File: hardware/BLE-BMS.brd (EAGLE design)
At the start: 61 x 50.8 mm, 88 parts, among them Q1 BSS138, U1 BQ7694040

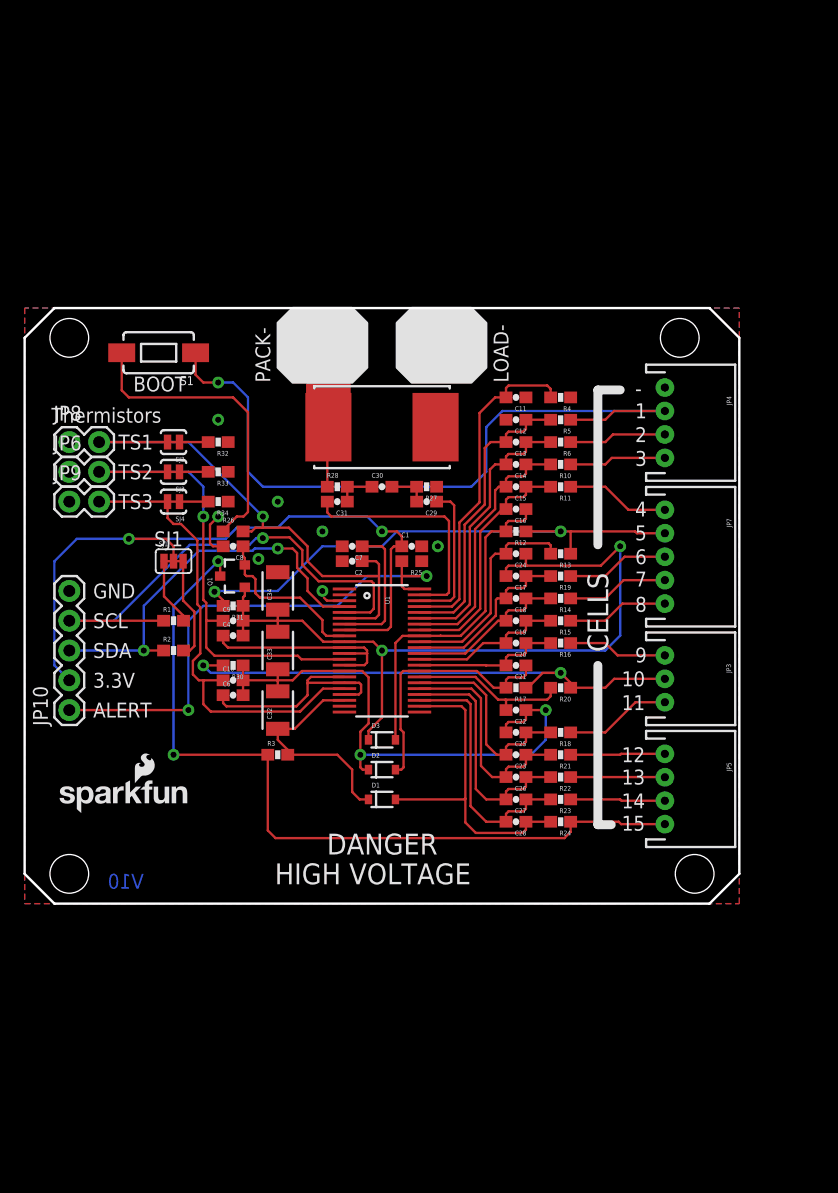
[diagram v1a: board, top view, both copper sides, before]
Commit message: v2 with Charge/Discharge MOSFET control and cell balancing
Many changes. Added large MOSFETs and pack interface circuitry. Added
small MOSFETs for individual cell balancing/charging. Corrected
Thermistor pull down error. All FPs pass 1:1 check.
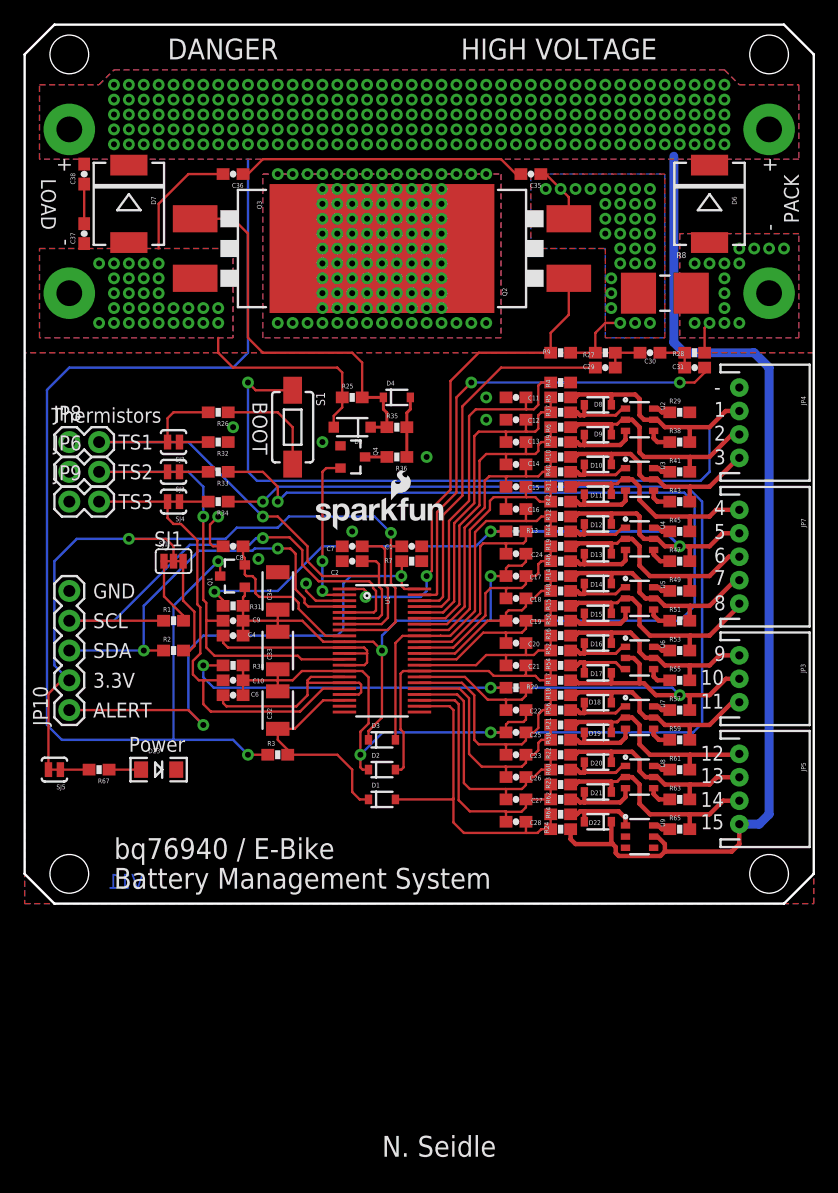
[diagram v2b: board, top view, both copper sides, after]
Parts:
- added C35, C36, C37, C38: 0.1uF, SparkFun-Capacitors:0603-CAP
- added D10, D11, D12, D13, D14, D15, D16, D17, D18, D19, D20, D21, D22, D8, D9: 5.6V, SparkFun-DiscreteSemi:SOD-323
- added D23: RED, SparkFun-LED:LED-1206
- added D4: BAS16, SparkFun-DiscreteSemi:SOD-323
- added D5: MMSZ5246B-7-F, SparkFun-DiscreteSemi:SOD-123
- added D6: SMCJ75AFS, SparkFun-DiscreteSemi:SMC
- added D7: ES3J, SparkFun-DiscreteSemi:SMC
- added Q2, Q3: PSMN7R0-100BS, SparkFun-DiscreteSemi:TO-263/D2PAK
- added Q4: 30V, 2.5A, SparkFun-DiscreteSemi:SOT23-3
- added R35, R7, R9: 1M, SparkFun-Resistors:0603-RES
- added R36, R67: 1K, SparkFun-Resistors:0603-RES
- added R37, R39, R40, R42, R44, R46, R48, R50, R52, R54, R56, R58, R60, R62, R64: 10K, SparkFun-Resistors:0603-RES
- added R38, R41, R43, R45, R47, R49, R51, R53, R55, R57, R59, R61, R63, R65: 100/.25W, SparkFun-Resistors:0603-RES
- added R8: CSR2512C0R001F, bq769x0:2512
- added SJ5: (no value), SparkFun-Passives:PAD-JUMPER-2-NC_BY_TRACE_YES_SILK
- added U2, U3, U4, U5, U6, U7, U8, U9: DMP2240, SparkFun-DiscreteSemi:SOT26
- R25: value 4.7k -> 1M; device SparkFun-Resistors:0603 -> SparkFun-Resistors:0603-RES
- R26: device SparkFun-Resistors:0603 -> SparkFun-Resistors:0603-RES
- R29: value .001 -> 100/.25W; device bq769x0:4527 -> SparkFun-Resistors:0603-RES
- U1: value BQ7694040 -> bq7694002DBT
- moved U$7 59.3 mm to (13.6, 2.08)
- moved C31 32.6 mm to (57.1, 45.7), turned to 0 degrees
- moved R28 32.6 mm to (57.1, 47.0), turned to 180 degrees
- moved LOGO1 32.5 mm to (24.4, 31.8)
- moved C30 25.6 mm to (53.3, 47.0), turned to 180 degrees
- moved R29 25.4 mm to (55.9, 41.9), turned to 0 degrees
- moved STANDOFF4 25.3 mm to (63.5, 72.4)
- moved STANDOFF3 24.2 mm to (3.81, 72.4)
- moved C29 19.1 mm to (49.5, 45.7), turned to 0 degrees
- moved R27 19.1 mm to (49.5, 47.0), turned to 0 degrees
- moved R25 14.9 mm to (27.9, 43.2), turned to 0 degrees
- moved S1 13.1 mm to (22.9, 40.6), turned to 270 degrees
- moved R26 10.2 mm to (16.5, 41.9), turned to 180 degrees
- moved JP3 6.35 mm to (61.0, 19.2)
- moved JP4 6.35 mm to (61.0, 41.0)
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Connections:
- removed net PACK-: R28.1, R29.2
- new net CHG_CTL: D4.C, D5.C, Q3.1, R25.2, R35.1
- new net LOAD-: C36.2, C37.1, D5.A, D7.A, Q3.3, R25.1
- new net LOAD1: Q2.2, Q3.2
- new net LOAD2: C35.1, Q2.3, R27.1, R8.1, R9.1
- new net N$1: D8.A, R37.1, U2.G1
- new net N$12: D10.A, R40.1, U3.G1
- new net N$13: R41.1, U3.D1
- new net N$14: D11.A, R42.1, U3.G2
- new net N$16: R43.1, U3.D2
- new net N$18: D12.A, R44.1, U4.G1
- new net N$19: R45.1, U4.D1
- new net N$2: Q4.3, R36.2
- new net N$20: D13.A, R46.1, U4.G2
- new net N$21: R47.1, U4.D2
- new net N$23: R49.1, U5.D1
- new net N$25: D14.A, R48.1, U5.G1
- new net N$26: R51.1, U5.D2
- new net N$27: D15.A, R50.1, U5.G2
- new net N$37: R53.1, U6.D1
- new net N$38: D16.A, R52.1, U6.G1
- new net N$39: D17.A, R54.1, U6.G2
- new net N$4: R29.1, U2.D1
- new net N$41: R55.1, U6.D2
- new net N$42: D18.A, R56.1, U7.G1
- new net N$43: R57.1, U7.D1
- new net N$44: D19.A, R58.1, U7.G2
- new net N$46: R59.1, U7.D2
- new net N$47: D20.A, R60.1, U8.G1
- new net N$5: D9.A, R39.1, U2.G2
- new net N$50: R61.1, U8.D1
- new net N$51: D21.A, R62.1, U8.G2
- new net N$52: R63.1, U8.D2
- new net N$53: D22.A, R64.1, U9.G1
- new net N$54: R65.1, U9.D1
- new net N$57: D23.A, R67.1
- new net N$58: R67.2, SJ5.1
- new net N$6: C35.2, C36.1
- new net N$7: D4.A, R35.2, R36.1
- new net N$8: R38.1, U2.D2
- new net N$9: C37.2, C38.1
- net ALERT: now also R7.2; no longer R25.2
- net CELL1: now also D8.C, R38.2, U2.S1
- net CELL10: now also D17.C, R57.2, U6.S2
- net CELL11: now also D18.C, R59.2, U7.S1
- net CELL12: now also D19.C, R61.2, U7.S2
- net CELL13: now also D20.C, R63.2, U8.S1
- net CELL14: now also D21.C, R65.2, U8.S2
- net CELL2: now also D9.C, R41.2, U2.S2
- net CELL3: now also D10.C, R43.2, U3.S1
- net CELL4: now also D11.C, R45.2, U3.S2
- net CELL5: now also D12.C, R47.2, U4.S1
- net CELL6: now also D13.C, R49.2, U4.S2
- net CELL7: now also D14.C, R51.2, U5.S1
- net CELL8: now also D15.C, R53.2, U5.S2
- net CELL9: now also D16.C, R55.2, U6.S1
- net CHG: now also Q4.2
- net DSG: now also Q2.1, R9.2
- net GND: now also D23.C, D6.A, Q4.1, R28.1, R29.2, R7.1, R8.2; no longer R25.1, R27.1, R29.1, R33.1, R34.1
- net PACK+: now also C38.2, D22.C, D6.C, D7.C, U9.S1
- net REGOUT: now also SJ5.2
- net VC1: now also R37.2
- net VC10: now also R54.2
- net VC10X: now also R34.1
- net VC11: now also R56.2
- net VC12: now also R58.2
- net VC13: now also R60.2
- net VC14: now also R62.2
- net VC15: now also R64.2
- net VC2: now also R39.2
- net VC3: now also R40.2
- net VC4: now also R42.2
- net VC5: now also R44.2
- net VC5X: now also R33.1
- net VC6: now also R46.2
- net VC7: now also R48.2
- net VC8: now also R50.2
- net VC9: now also R52.2
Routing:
- net PACK+: track 69.2 -> 189.5 mm, vias 2 -> 214
- net VC10X: track 48.3 -> 119.8 mm, vias 2 -> 3
- net VC5X: track 67.8 -> 115.7 mm, vias 2 -> 3
- net DSG: track 0.00 -> 43.1 mm, vias 0 -> 2
- net CHG_CTL: track 0.00 -> 33.4 mm
- net LOAD-: track 0.00 -> 27.9 mm, vias 0 -> 31
- net N$6: track 0.00 -> 24.8 mm
- net CELL10: track 45.9 -> 68.2 mm, vias 2 -> 3
- net SRN: track 20.3 -> 41.4 mm, vias 0 -> 2
- net SRP: track 12.9 -> 31.8 mm
- net CELL5: track 47.0 -> 64.6 mm, vias 2 -> 3
- net N$32: track 26.1 -> 9.18 mm
- net CELL1: track 62.8 -> 77.8 mm
- net CHG: track 0.00 -> 13.8 mm, vias 0 -> 2
- net CELL2: track 8.31 -> 20.2 mm
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- added copper zone on layer 1, net LOAD-
- added copper zone on layer 16, net LOAD-
- added copper zone on layer 1, net LOAD1
- added copper zone on layer 16, net LOAD1
- added copper zone on layer 1, net LOAD2
- added copper zone on layer 16, net LOAD2
- added copper zone on layer 1, net PACK+
- added copper zone on layer 16, net PACK+
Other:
- board size 61 x 50.8 mm -> 67.3 x 75 mm
- board text added: "+"
- board text added: "Battery Management System"
- board text added: "LOAD"
- board text added: "N. Seidle"
- board text added: "PACK"
- board text added: "Power"
- board text added: "V11"
- board text added: "bq76940 / E-Bike"
- board text removed: "LOAD-"
- board text removed: "PACK-"
- board text removed: "V10"
